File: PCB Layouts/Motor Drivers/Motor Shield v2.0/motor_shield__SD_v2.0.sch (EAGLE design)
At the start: 26 parts

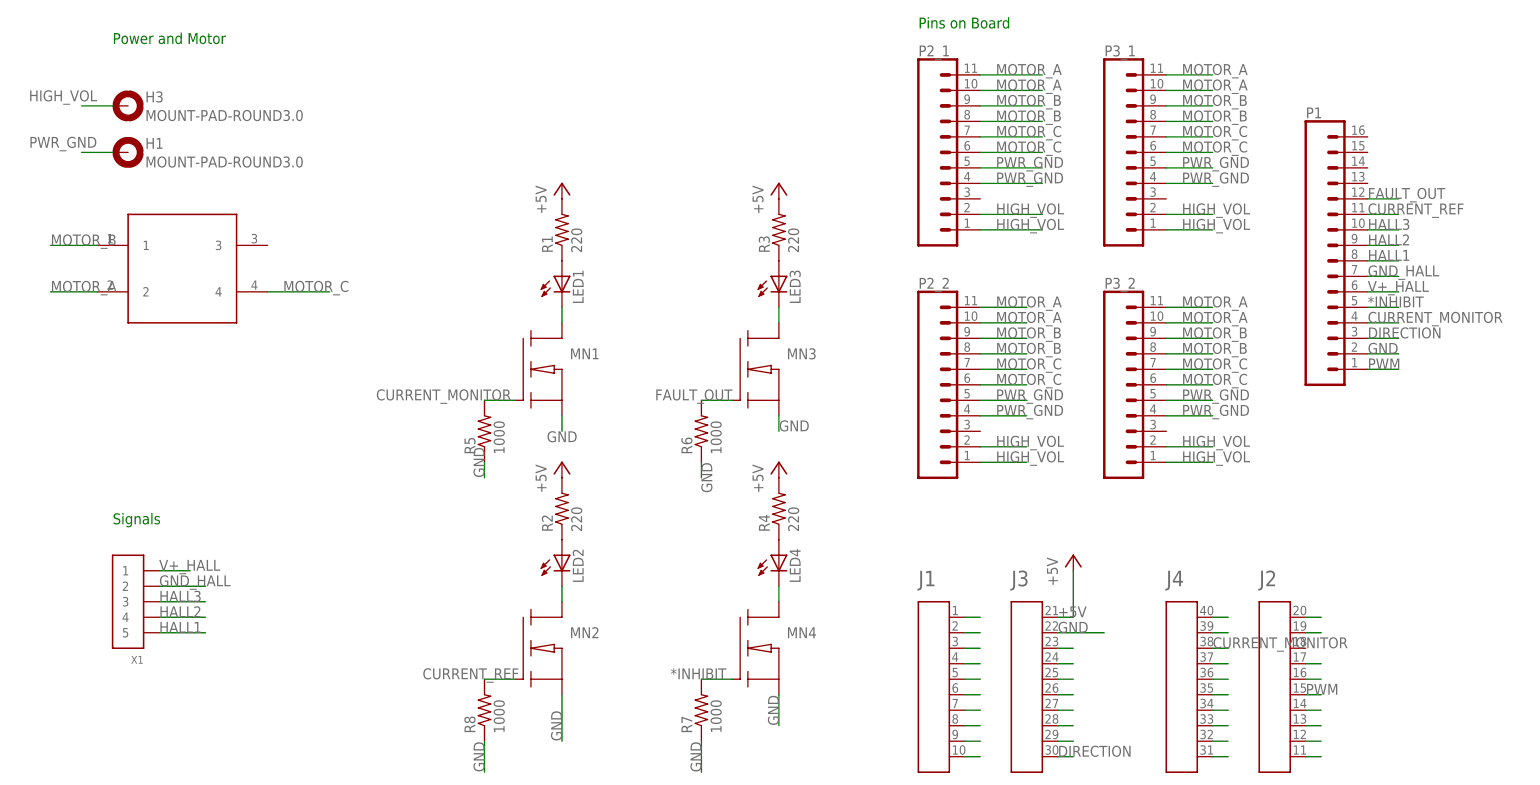
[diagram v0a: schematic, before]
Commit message: Testing force control PID
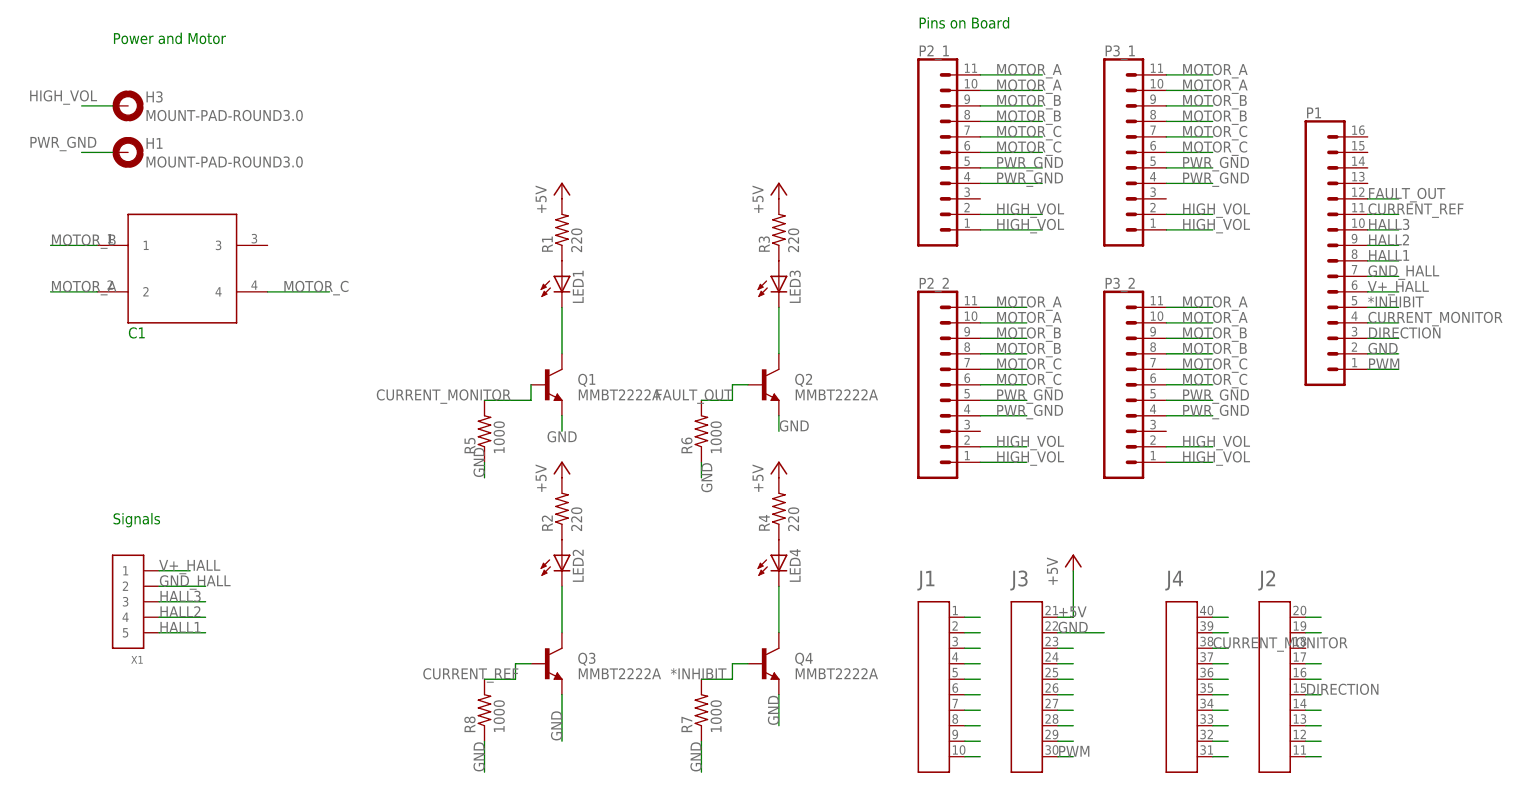
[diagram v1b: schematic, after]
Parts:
- removed MN1, MN2, MN3, MN4: (no value), sym:NMOS
- added Q1, Q2, Q3, Q4: MMBT2222A, SparkFun-DiscreteSemi:TRANSISTOR_NPNMMBT2222A
- renumbered U$2 to C1
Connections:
- net *INHIBIT: now also Q4.B; no longer MN4.G
- net CURRENT_MONITOR: now also Q1.B; no longer MN1.G
- net CURRENT_REF: now also Q3.B; no longer MN2.G
- net DIRECTION: now also A1.P$15; no longer A1.P$30
- net FAULT_OUT: now also Q2.B; no longer MN3.G
- net GND: now also Q1.E, Q2.E, Q3.E, Q4.E; no longer MN1.S, MN2.S, MN3.S, MN4.S
- net N$15: now also Q1.C; no longer MN1.D
- net N$16: now also Q3.C; no longer MN2.D
- net N$30: now also Q2.C; no longer MN3.D
- net N$41: now also Q4.C; no longer MN4.D
- net PWM: now also A1.P$30; no longer A1.P$15
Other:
- note added: "C1"

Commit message: Tiva shield
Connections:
- removed net N$51: A1.P$6
- net CURRENT_MONITOR: now also A1.P$6; no longer A1.P$38
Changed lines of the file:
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@@
 </segment>
 <segment>
-<pinref part="A1" gate="G$1" pin="P$38"/>
-<wire x1="205.74" y1="73.66" x2="208.28" y2="73.66" width="0.1524" layer="91"/>
-<label x="205.74" y="73.66" size="1.778" layer="95"/>
+<pinref part="A1" gate="G$1" pin="P$6"/>
+<wire x1="165.1" y1="66.04" x2="167.64" y2="66.04" width="0.1524" layer="91"/>
+<label x="165.1" y="66.04" size="1.778" layer="95"/>
 </segment>
 </net>
@@
 </segment>
 </net>
-<net name="N$51" class="0">
-<segment>
-<pinref part="A1" gate="G$1" pin="P$6"/>
-<wire x1="165.1" y1="66.04" x2="167.64" y2="66.04" width="0.1524" layer="91"/>
-</segment>
-</net>
